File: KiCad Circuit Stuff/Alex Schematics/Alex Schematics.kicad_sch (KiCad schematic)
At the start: 0 parts

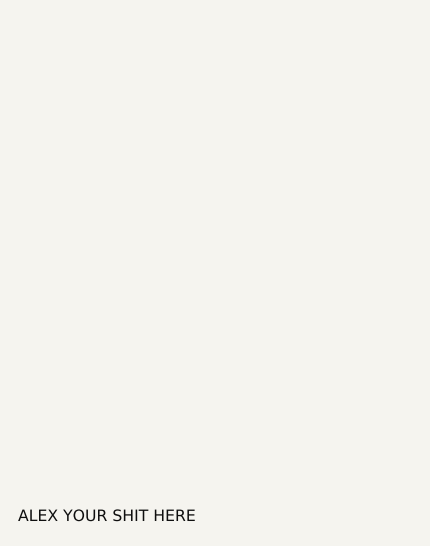
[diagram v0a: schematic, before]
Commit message: I added a driver IC
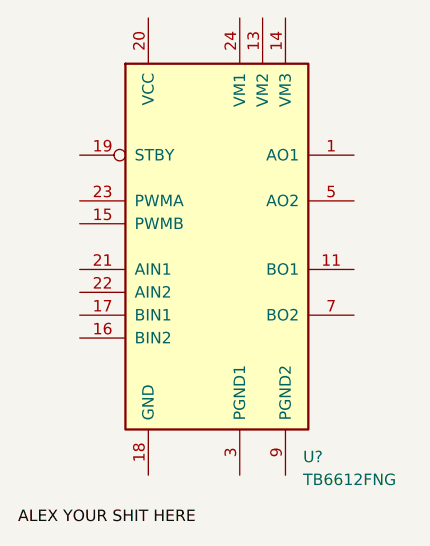
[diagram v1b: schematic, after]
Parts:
- added U?: TB6612FNG, Package_SO:SSOP-24_5.3x8.2mm_P0.65mm, symbol Driver_Motor:TB6612FNG
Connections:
- new net: U?.1 (AO1), U?.2 (AO1)
- new net: U?.10 (PGND2), U?.9 (PGND2)
- new net: U?.11 (BO1), U?.12 (BO1)
- new net: U?.3 (PGND1), U?.4 (PGND1)
- new net: U?.5 (AO2), U?.6 (AO2)
- new net: U?.7 (BO2), U?.8 (BO2)
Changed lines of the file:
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@@
     (effects (font (size 1.27 1.27)) (justify left bottom))
+  )
+  (symbol (lib_id "Driver_Motor:TB6612FNG") (at 146.558 56.642 0) (unit 1)
+    (in_bom yes) (on_board yes) (dnp no) (fields_autoplaced)
+    (property "Reference" "U?" (at 156.1339 80.01 0)
+      (effects (font (size 1.27 1.27)) (justify left))
+    )
+    (property "Value" "TB6612FNG" (at 156.1339 82.55 0)
+      (effects (font (size 1.27 1.27)) (justify left))
+    )
+    (property "Footprint" "Package_SO:SSOP-24_5.3x8.2mm_P0.65mm" (at 179.578 79.502 0)
+      (effects (font (size 1.27 1.27)) hide)
+    )
+    (property "Datasheet" "https://toshiba.semicon-storage.com/us/product/linear/motordriver/detail.TB6612FNG.html" (at 157.988 41.402 0)
+      (effects (font (size 1.27 1.27)) hide)
+    )
+    (pin "1")
+    (pin "10")
+    (pin "11")
+    (pin "12")
+    (pin "13")
+    (pin "14")
+    (pin "15")
+    (pin "16")
+    (pin "17")
+    (pin "18")
+    (pin "19")
+    (pin "2")
+    (pin "20")
+    (pin "21")
+    (pin "22")
+    (pin "23")
+    (pin "24")
+    (pin "3")
+    (pin "4")
+    (pin "5")
+    (pin "6")
+    (pin "7")
+    (pin "8")
+    (pin "9")
+    (instances
+      (project "Alex Schematics"
+        (path "/283256c9-17c0-4062-8970-b31f914079db"
+          (reference "U?") (unit 1)
+        )
+      )
+    )
   )
   (sheet_instances

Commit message: added some stuff
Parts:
- removed U?: TB6612FNG, Package_SO:SSOP-24_5.3x8.2mm_P0.65mm, symbol Driver_Motor:TB6612FNG
- added C1, C2, C3, C4: 0.1uF, symbol Device:C_Small
- added C10, C5, C6, C7, C8, C9: 1uF, symbol Device:C_Small
- added C5: 10uF, symbol Device:C_Small
- added J1 (x2): Conn_02x16_Odd_Even, symbol Connector_Generic:Conn_02x16_Odd_Even
- added R?: 10k, symbol Device:R_Small
- added U1, U2: DRV8833PWP, DRV8833_NEW:TSSOP-16_L5.0-W4.4-P0.65-LS6.4-BL-EP, symbol DRV8833_NEW:DRV8833PWP
- added U1, U2: TB6612FNG, Package_SO:SSOP-24_5.3x8.2mm_P0.65mm, symbol Driver_Motor:TB6612FNG
- added U4: TYPE-C_16P_QTGM027, DRV8833_NEW:USB-C-SMD_TYPE-C-16P-QTGM027, symbol TYPE-C 16P QTGM027:TYPE-C_16P_QTGM027
- added U5: HUSB237-AA001-DN06R, DRV8833_NEW:TDFN-6_L2.0-W2.0-P0.65-TL-EP, symbol HUSB237_NEW:HUSB237-AA001-DN06R
- added U6, U7, U8: AP22814AW5-7, DRV8833_NEW:SOT-25_L3.0-W1.6-P0.95-LS2.8-BL, symbol AP22814AW5-7:AP22814AW5-7
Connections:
- new net: C8.2, U6.1 (OUT)
- new net: C9.2, U8.5 (IN)
- new net: R?.1, U5.3 (VSET)
- new net: C2.1, U1.11 (VCP)
- new net: C1.1, C2.2, U1.14 (VINT)
- new net: C7.2, U7.1 (OUT)
- new net: C6.1, U7.5 (IN)
- new net: C5.1, U6.5 (IN)
- new net: J1.27 (Pin_27), U2.1 (AO1), U2.2 (AO1)
- new net: J1.23 (Pin_23), U1.10 (PGND2), U1.3 (PGND1), U1.4 (PGND1), U1.9 (PGND2), U2.10 (PGND2), U2.3 (PGND1), U2.4 (PGND1), U2.9 (PGND2)
- new net: J1.3 (Pin_3), U2.11 (BO1), U2.12 (BO1)
- new net: J1.14 (Pin_14), U1.13 (VM2), U1.14 (VM3), U1.24 (VM1), U2.13 (VM2), U2.14 (VM3), U2.24 (VM1)
- new net: J1.10 (Pin_10), U2.16 (BIN2)
- new net: J1.8 (Pin_8), U2.17 (BIN1)
- new net: J1.19 (Pin_19), U1.18 (GND), U2.18 (GND)
- new net: J1.18 (Pin_18), U1.20 (VCC), U2.20 (VCC)
- new net: J1.24 (Pin_24), U2.21 (AIN1)
- new net: J1.26 (Pin_26), U2.22 (AIN2)
- new net: J1.29 (Pin_29), U2.5 (AO2), U2.6 (AO2)
- new net: J1.5 (Pin_5), U2.7 (BO2), U2.8 (BO2)
- new net: C3.1, U2.14 (VINT)
- new net: J1.1 (Pin_1), U1.7 (BO2), U1.8 (BO2)
- new net: J1.2 (Pin_2), U1.11 (BO1), U1.12 (BO1)
- new net: J1.28 (Pin_28), U1.21 (AIN1)
- new net: J1.30 (Pin_30), U1.22 (AIN2)
- new net: J1.31 (Pin_31), U1.5 (AO2), U1.6 (AO2)
- new net: J1.32 (Pin_32), U1.1 (AO1), U1.2 (AO1)
- new net: J1.4 (Pin_4), U1.17 (BIN1)
- new net: J1.6 (Pin_6), U1.16 (BIN2)
- new net: C4.1, U2.11 (VCP)
- new net +3V3: J1.18 (Pin_18), U1.1 (nSleep), U2.1 (nSleep)
- new net AIN1 (U1): J1.28 (Pin_28)
- new net AIN1 (U2): J1.8 (Pin_8)
- new net AIN2 (U1): J1.30 (Pin_30)
- new net AIN2 (U2): J1.10 (Pin_10)
- new net AOUT1 (U1): J1.32 (Pin_32)
- new net AOUT1 (U2): J1.3 (Pin_3)
- new net AOUT2 (U1): J1.31 (Pin_31)
- new net AOUT2 (U2): J1.5 (Pin_5)
- new net BIN1 (U1): J1.4 (Pin_4)
- new net BIN1 (U2): J1.24 (Pin_24)
- new net BIN2 (U1): J1.6 (Pin_6)
- new net BIN2 (U2): J1.26 (Pin_26)
- new net BOUT1 (U1): J1.2 (Pin_2)
- new net BOUT1 (U2): J1.27 (Pin_27)
- new net BOUT2 (U1): J1.1 (Pin_1)
- new net BOUT2 (U2): J1.29 (Pin_29)
- new net CC1: U4.A5 (CC1), U5.1 (CC1)
- new net CC2: U4.B5 (CC2), U5.6 (CC2)
- new net DN1: U4.B7 (DN2)
- new net DN1/DN2: U5.5 (D-)
- new net DN2: U4.A7 (DN1)
- new net DP1: U4.B6 (DP2)
- new net DP1/DP2: U5.4 (D+)
- new net DP2: U4.A6 (DP1)
- new net EN_LOAD1: U6.4 (EN)
- new net EN_LOAD2: U7.4 (EN)
- new net GND: C1.2, C10.1, C3.2, C4.2, C5.1, C5.2, C5.2, C6.2, C7.1, C8.1, C9.1, J1.13 (Pin_13), J1.19 (Pin_19), R?.2, U1.12 (VM), U1.13 (GND), U1.17 (GND), U1.3 (AISEN), U1.6 (BISEN), U2.12 (VM), U2.13 (GND), U2.17 (GND), U2.3 (AISEN), U2.6 (BISEN), U4.17 (EH), U4.18 (EH), U4.19 (EH), U4.20 (EH), U4.A1 (GND), U4.A12 (GND), U5.7 (GND), U6.2 (GND), U7.2 (GND), U8.1 (OUT), U8.2 (GND)
- new net MOTOR1_A_OUT: U1.2 (AOUT1)
- new net MOTOR1_B_OUT: U1.4 (AOUT2)
- new net MOTOR1_CTRL1: U1.16 (AIN1)
- new net MOTOR1_CTRL2: U1.15 (AIN2)
- new net MOTOR2_A_OUT: U1.7 (BOUT1)
- new net MOTOR2_B_OUT: U1.5 (BOUT2)
- new net MOTOR2_CTRL1: U1.9 (BIN1)
- new net MOTOR2_CTRL2: U1.10 (BIN2)
- new net MOTOR3_A_OUT: U2.7 (BOUT1)
- new net MOTOR3_B_OUT: U2.5 (BOUT2)
- new net MOTOR3_CTRL1: U2.9 (BIN1)
- new net MOTOR3_CTRL2: U2.10 (BIN2)
- new net MOTOR4_A_OUT: U2.2 (AOUT1)
- new net MOTOR4_B_OUT: U2.4 (AOUT2)
- new net MOTOR4_CTRL1: U2.16 (AIN1)
- new net MOTOR4_CTRL2: U2.15 (AIN2)
- new net PWM Pin (TIM3_CH3): U1.23 (PWMA)
- new net PWM Pin (TIM4_CH1): U1.15 (PWMB)
- new net VBUS: U4.A4 (VBUS), U4.A9 (VBUS), U5.2 (VUSB)
- new net VIN_MT6308: C10.2
- new net VM: J1.14 (Pin_14)
- no-connect marks 0 -> 4
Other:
- note added: "1 Motor2_B_OUT 2 Motor2_A_OUT 3 Motor4_A_OUT 4 PD12/TIM4C1 MOTOR2_CTRL1 5 Motor4_B_OUT 6 PD13/TIM4C2 MOTOR2_CTRL2 7 PD2 CTRL_EXT_LOAD2 8 PD14/TIM4C3 MOTOR4_CTRL1 9 PD6/RESV USART2_RX 10 PD15/TIM4C4 MOTOR4_CTRL2 11 EXT_LOAD2_OUT 12 PD5/RESV USART2_TX 13 PB4 FAST_CHARGE_CTRL 14 Battery 15 PD7/ RESV 16 PB8 I2C1_SCL 17 PB9 I2C1_SDA 18 3V3 Out 19 GND 20 5V Out 21 EXT_LOAD1_OUT 22 HV HV 23 GND 24 PC6/T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"
- note added: "Driver IC (1) - 2 x Brushed Motors (400mA)"
- note added: "EN - either needs GPIO Control or a pull-up + switch"
- note added: "U1 controls the two 200mA motors (Motor 1 and 2)"
- note added: "U2 controls the two 500mA auxiliary motors (Motor 3 and 4)"
- note added: "can be 1uF for OUT"

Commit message: added some stuff
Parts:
- removed C5: 10uF, symbol Device:C_Small
- removed J1: Conn_02x16_Odd_Even, symbol Connector_Generic:Conn_02x16_Odd_Even
- removed U1, U2: TB6612FNG, Package_SO:SSOP-24_5.3x8.2mm_P0.65mm, symbol Driver_Motor:TB6612FNG
- added C1, C10: 10uF, symbol Device:C_Small
- added C2: 2.2uF, symbol Device:C_Small
- added C3: 10nF, symbol Device:C_Small
- added J?: Conn_02x16_Odd_Even, symbol Connector_Generic:Conn_02x16_Odd_Even
- added U?: DRV8833PWP, DRV8833_NEW:TSSOP-16_L5.0-W4.4-P0.65-LS6.4-BL-EP, symbol DRV8833_NEW:DRV8833PWP
- C3: value 0.1uF -> 2.2uF
- C4: value 0.1uF -> 0.01uF
- gave numbers to parts that had none: 1
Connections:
- net +3V3: now also U?.1 (nSleep)
- net GND: now also C1.2, C10.1, C10.2, C2.2
- net MOTOR1_A_OUT: now also U?.2 (AOUT1)
- net MOTOR1_B_OUT: now also U?.4 (AOUT2)
- net MOTOR1_CTRL1: now also U?.16 (AIN1)
- net MOTOR1_CTRL2: now also U?.15 (AIN2)
- net MOTOR2_A_OUT: now also U?.7 (BOUT1)
- net MOTOR2_B_OUT: now also U?.5 (BOUT2)
- net MOTOR2_CTRL1: now also U?.9 (BIN1)
- net MOTOR2_CTRL2: now also U?.10 (BIN2)
- new net: C3.1, U?.11 (VCP)
- new net: C2.1, U?.14 (VINT)
- new net 5V OUT: C1.1, C3.2, U?.12 (VM)
- no-connect marks 4 -> 0
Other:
- note removed: "Driver IC (1) - 2 x Brushed Motors (400mA)"
